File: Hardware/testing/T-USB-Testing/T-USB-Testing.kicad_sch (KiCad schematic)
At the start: 5 parts

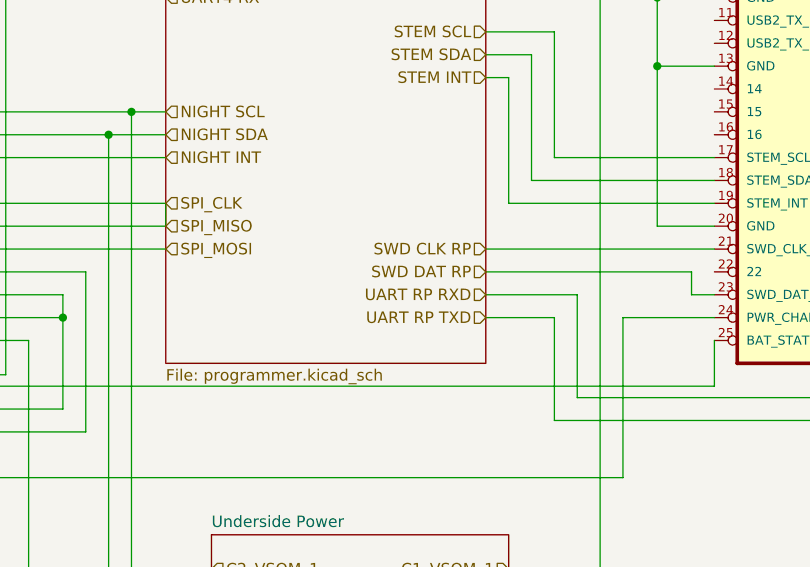
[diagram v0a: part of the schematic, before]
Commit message: MSP debug pins tweaks
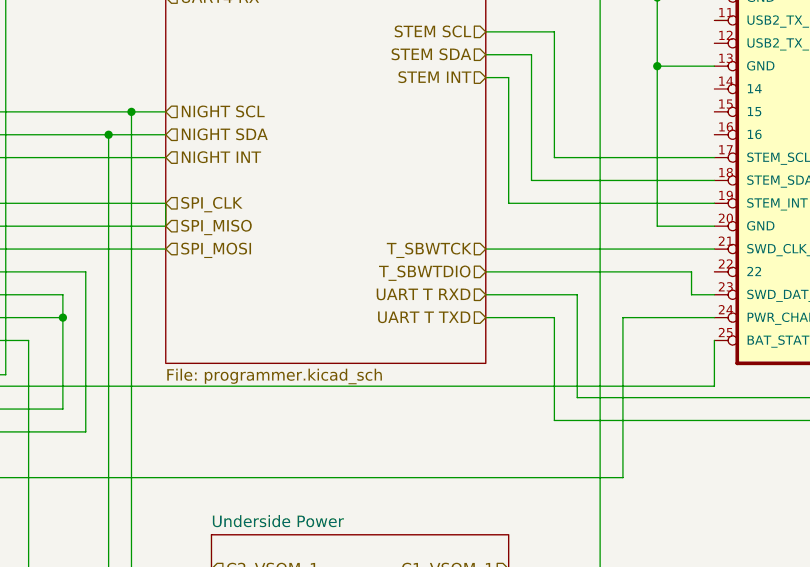
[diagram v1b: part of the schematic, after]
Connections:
- net SWD CLK RP renamed T_SBWTCK
- net SWD DAT RP renamed T_SBWTDIO
- net UART RP RXD renamed UART T RXD
- net UART RP TXD renamed UART T TXD
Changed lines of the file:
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@@
     (effects (font (size 1.27 1.27)) (justify left))
   )
-  (hierarchical_label "SWD CLK RP" (shape input) (at 147.32 81.28 180)
+  (hierarchical_label "T_SBWTCK" (shape input) (at 147.32 81.28 180)
     (effects (font (size 1.27 1.27)) (justify right))
   )
@@
     (effects (font (size 1.27 1.27)) (justify right))
   )
-  (hierarchical_label "UART RP TXD" (shape input) (at 147.32 88.9 180)
+  (hierarchical_label "UART T TXD" (shape input) (at 147.32 88.9 180)
     (effects (font (size 1.27 1.27)) (justify right))
   )
@@
     (effects (font (size 1.27 1.27)) (justify left))
   )
-  (hierarchical_label "UART RP RXD" (shape input) (at 147.32 86.36 180)
+  (hierarchical_label "UART T RXD" (shape input) (at 147.32 86.36 180)
     (effects (font (size 1.27 1.27)) (justify right))
   )
@@
     (effects (font (size 1.27 1.27)) (justify right))
   )
-  (hierarchical_label "SWD DAT RP" (shape input) (at 147.32 83.82 180)
+  (hierarchical_label "T_SBWTDIO" (shape input) (at 147.32 83.82 180)
     (effects (font (size 1.27 1.27)) (justify right))
   )
